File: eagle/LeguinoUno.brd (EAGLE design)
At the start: 68.2 x 53.3 mm, 34 parts, among them Q1 60V/32A/35m?, Q2 60V/32A/35m?, Q3 60V/32A/35m?, Q4 60V/32A/35m?, Q5 60V/32A/35m?

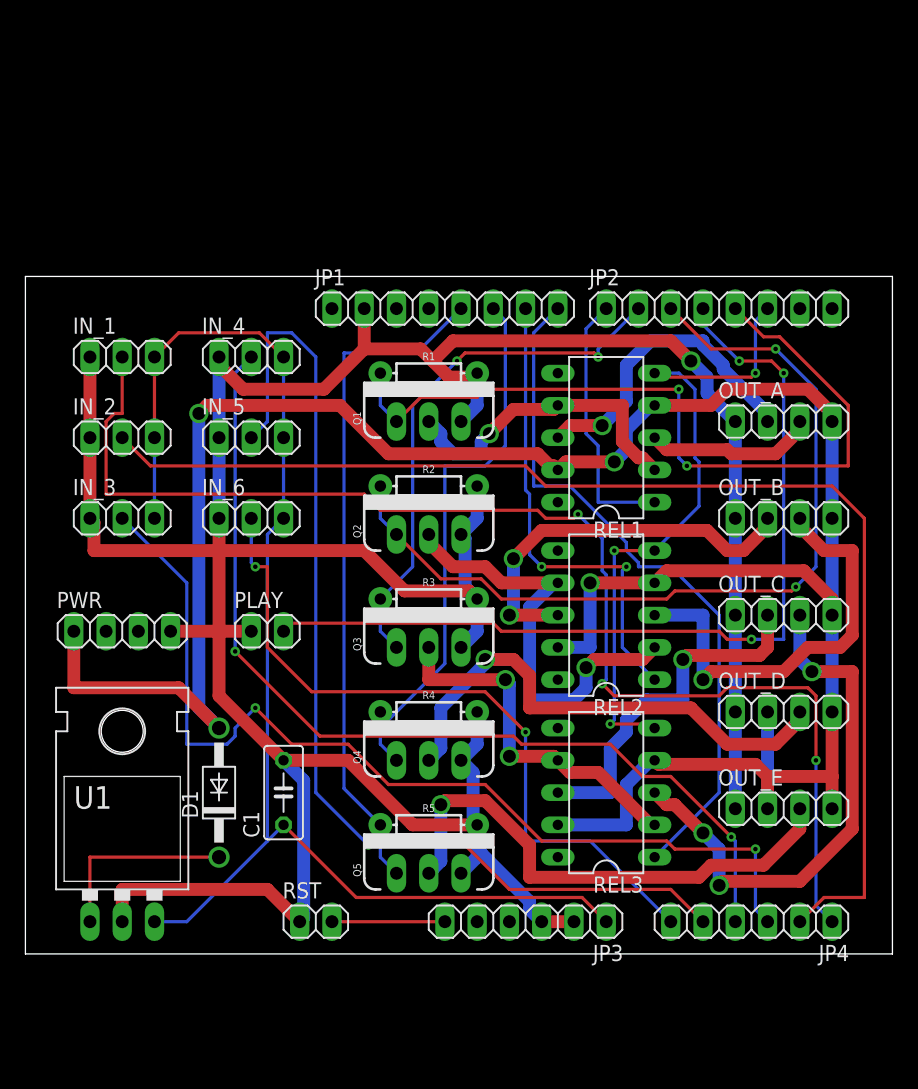
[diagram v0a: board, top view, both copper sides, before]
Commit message: Updated EAGLE schematics and board, moved EAGLE files to top-level, created Gerber files.
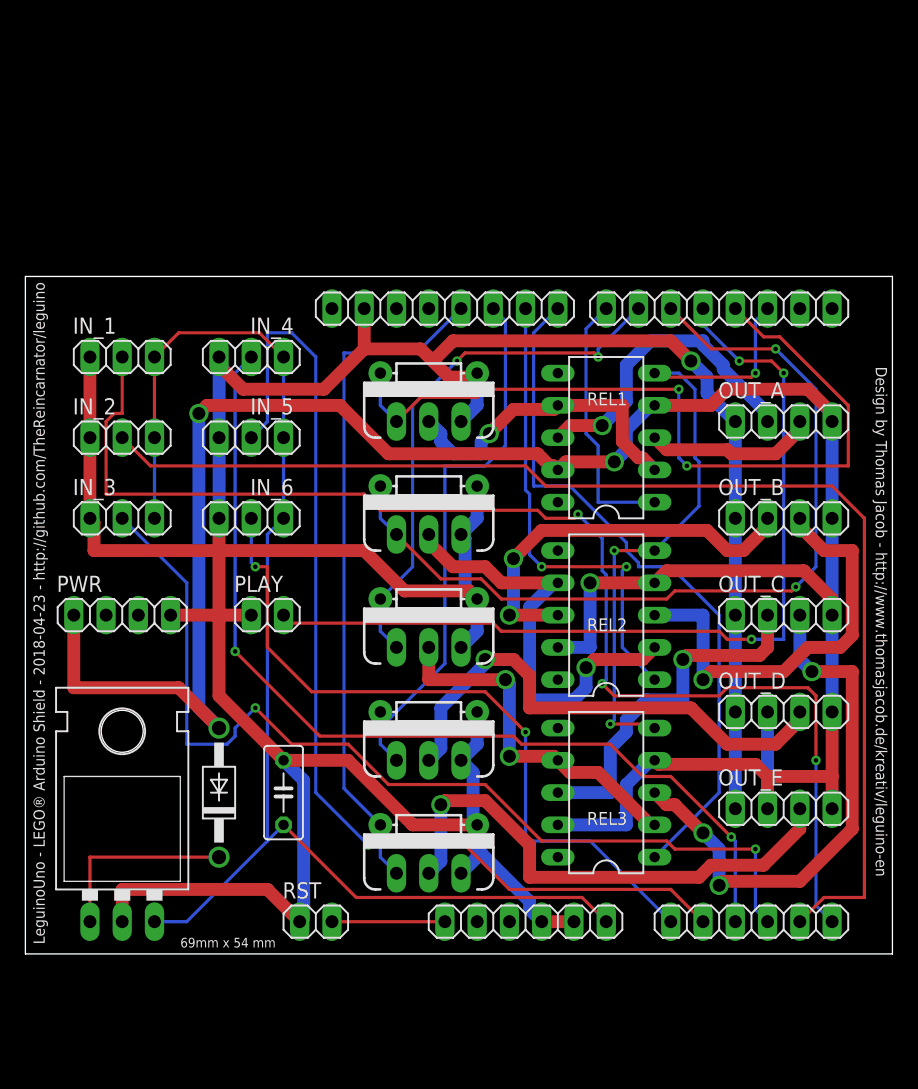
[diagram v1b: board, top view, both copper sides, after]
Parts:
- EZSBC_PSU2-5: value (none) -> EzSBC PSU2-5
- Q1, Q2, Q3, Q4, Q5: value 60V/32A/35m? -> FQP30N06L
- moved PLAY 1.27 mm to (59.7, 34.3)
- moved PWR 1.27 mm to (48.3, 34.3)
- renumbered U1 to EZSBC_PSU2-5
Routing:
- net V+: track 195.8 -> 197.1 mm
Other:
- board text added: "69mm x 54 mm"
- board text added: "Design by Thomas Jacob - http://www.thomasjacob.de/kreativ/leguino-en"
- board text added: "LeguinoUno - LEGO® Arduino Shield - 2018-04-23 - http://github.com/TheReincarnator/leguino"

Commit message: fix VCC Arduino connection and width, reroute
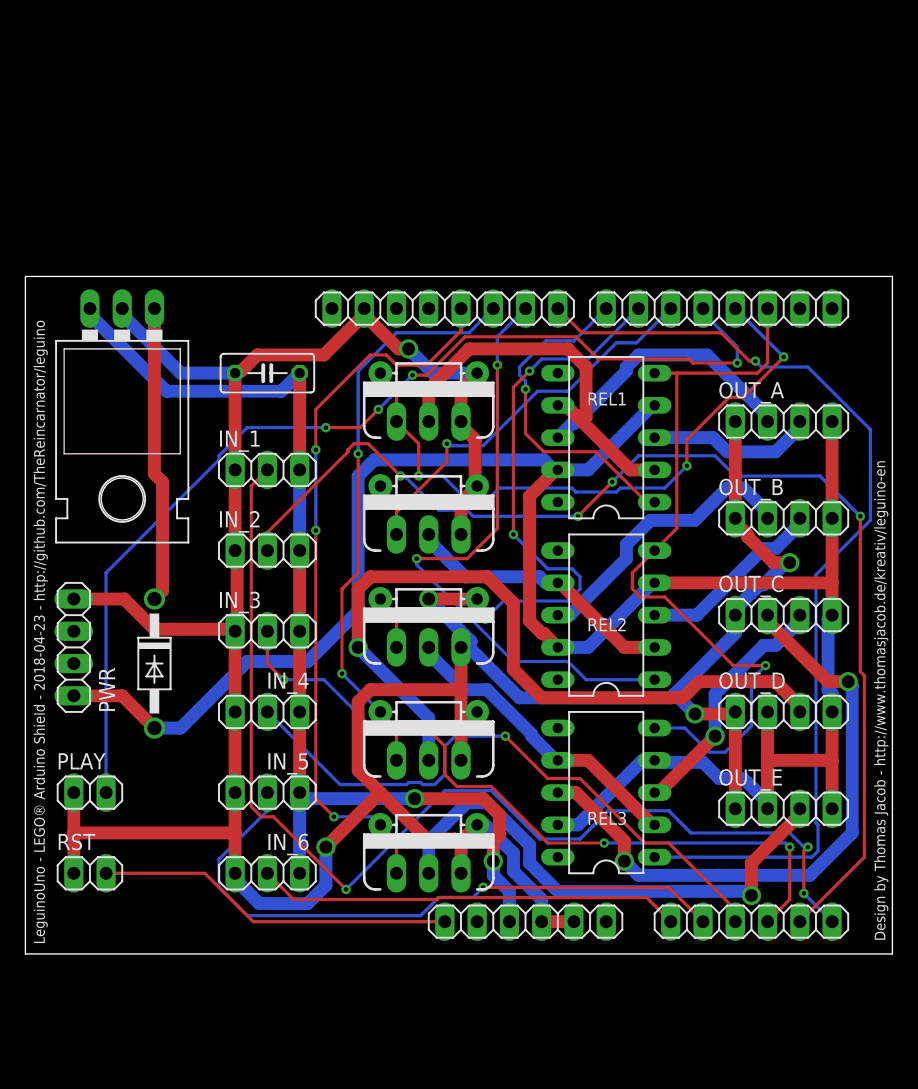
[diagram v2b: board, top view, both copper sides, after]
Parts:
- moved EZSBC_PSU2-5 40.6 mm to (48.3, 54.6), turned to 180 degrees
- moved C1 33.0 mm to (59.7, 53.3), turned to 180 degrees
- moved IN_4 28.0 mm to (59.7, 26.7)
- moved IN_5 28.0 mm to (59.7, 20.3)
- moved IN_6 28.0 mm to (59.7, 14.0)
- moved PLAY 19.8 mm to (45.7, 20.3)
- moved RST 18.2 mm to (45.7, 14.0)
- moved IN_1 14.5 mm to (59.7, 45.7)
- moved IN_2 14.5 mm to (59.7, 39.4)
- moved IN_3 14.5 mm to (59.7, 33.0)
- moved D1 11.4 mm to (50.8, 30.5), turned to 270 degrees
- moved PWR 4.58 mm to (44.5, 31.8), turned to 90 degrees
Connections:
- net VCC: now also JP3.4; no longer JP3.1
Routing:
- net UNO_D5: track 68.5 -> 33.5 mm, vias 2 -> 1
- net UNO_A4: track 82.4 -> 50.1 mm
- net V+: track 197.1 -> 167.7 mm, vias 3 -> 0
- net UNO_A3: track 75.6 -> 48.8 mm, vias 2 -> 1
- net UNO_A5: track 57.0 -> 33.5 mm, vias 2 -> 0
- net OUT_C-: track 42.5 -> 19.4 mm, vias 3 -> 1
- net UNO_D8: track 55.3 -> 76.6 mm, vias 0 -> 1
- net OUT_C+: track 28.2 -> 49.0 mm, vias 1 -> 2
- net VCC: track 104.9 -> 85.0 mm, vias 0 -> 2
- net OUT_D-: track 40.2 -> 59.8 mm
- net OUT_B-: track 34.3 -> 14.9 mm, vias 1 -> 0
- net UNO_A2: track 76.9 -> 57.5 mm, vias 2 -> 4
- net UNO_RST: track 8.89 -> 28.2 mm
- net N$13: track 34.9 -> 21.7 mm, vias 1 -> 0
- net UNO_A0: track 100.2 -> 87.4 mm
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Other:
- board text removed: "69mm x 54 mm"

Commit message: fix analog pin assignment for Uno
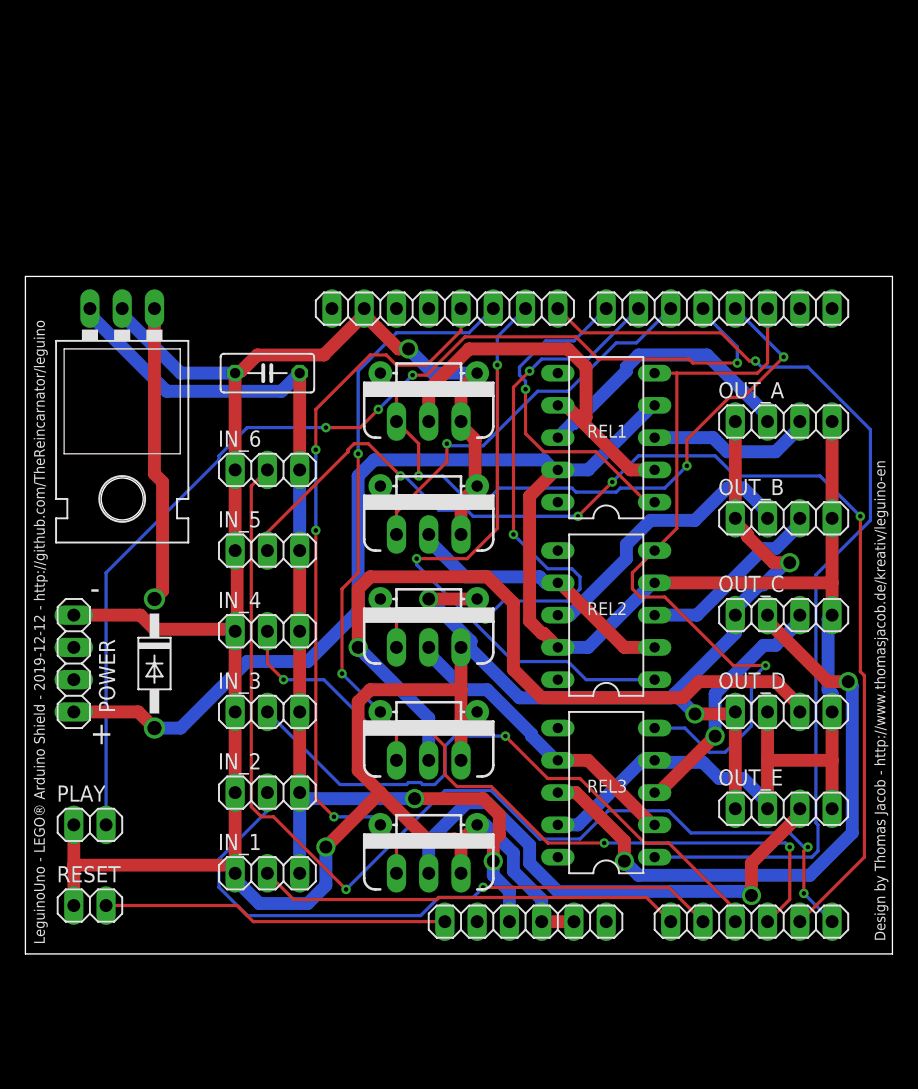
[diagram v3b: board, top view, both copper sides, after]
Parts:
- removed PWR: (no value), pinhead:1X04
- removed RST: (no value), pinhead:1X02
- added POWER: (no value), pinhead:1X04
- added RESET: (no value), pinhead:1X02
- moved IN_1 31.8 mm to (59.7, 14.0)
- moved IN_6 31.8 mm to (59.7, 45.7)
- moved IN_2 19.0 mm to (59.7, 20.3)
- moved IN_5 19.0 mm to (59.7, 39.4)
- moved IN_3 6.35 mm to (59.7, 26.7)
- moved IN_4 6.35 mm to (59.7, 33.0)
- moved PLAY 2.54 mm to (45.7, 17.8)
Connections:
- net GND: now also POWER.4, RESET.1; no longer PWR.4, RST.1
- net UNO_A0: now also JP4.6; no longer JP4.1
- net UNO_A1: now also JP4.5; no longer JP4.2
- net UNO_A2: now also JP4.4; no longer JP4.3
- net UNO_A3: now also JP4.3; no longer JP4.4
- net UNO_A4: now also JP4.2; no longer JP4.5
- net UNO_A5: now also JP4.1; no longer JP4.6
- net UNO_RST: now also RESET.2; no longer RST.2
- net V+: now also POWER.1; no longer PWR.1
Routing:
- net UNO_A5: track 33.5 -> 87.4 mm, vias 0 -> 3
- net UNO_A0: track 87.4 -> 33.5 mm, vias 3 -> 0
- net UNO_A4: track 50.1 -> 91.5 mm, vias 1 -> 4
- net UNO_A1: track 91.5 -> 50.1 mm, vias 4 -> 1
- net UNO_A3: track 48.8 -> 57.5 mm, vias 1 -> 4
- net UNO_A2: track 57.5 -> 48.8 mm, vias 4 -> 1
- net UNO_D4: track 81.1 -> 83.7 mm
- net UNO_RST: track 28.2 -> 27.2 mm
- net V+: track 167.7 -> 167.2 mm
- net GND: track 259.9 -> 259.4 mm
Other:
- board text added: "+"
- board text added: "-"
- board text added: "LeguinoUno - LEGO® Arduino Shield - 2019-12-12 - http://github.com/TheReincarnator/leguino"
- board text removed: "LeguinoUno - LEGO® Arduino Shield - 2018-04-23 - http://github.com/TheReincarnator/leguino"
